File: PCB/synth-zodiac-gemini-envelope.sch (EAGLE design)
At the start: 23 parts, among them Q1 PNP, U1 TL074A

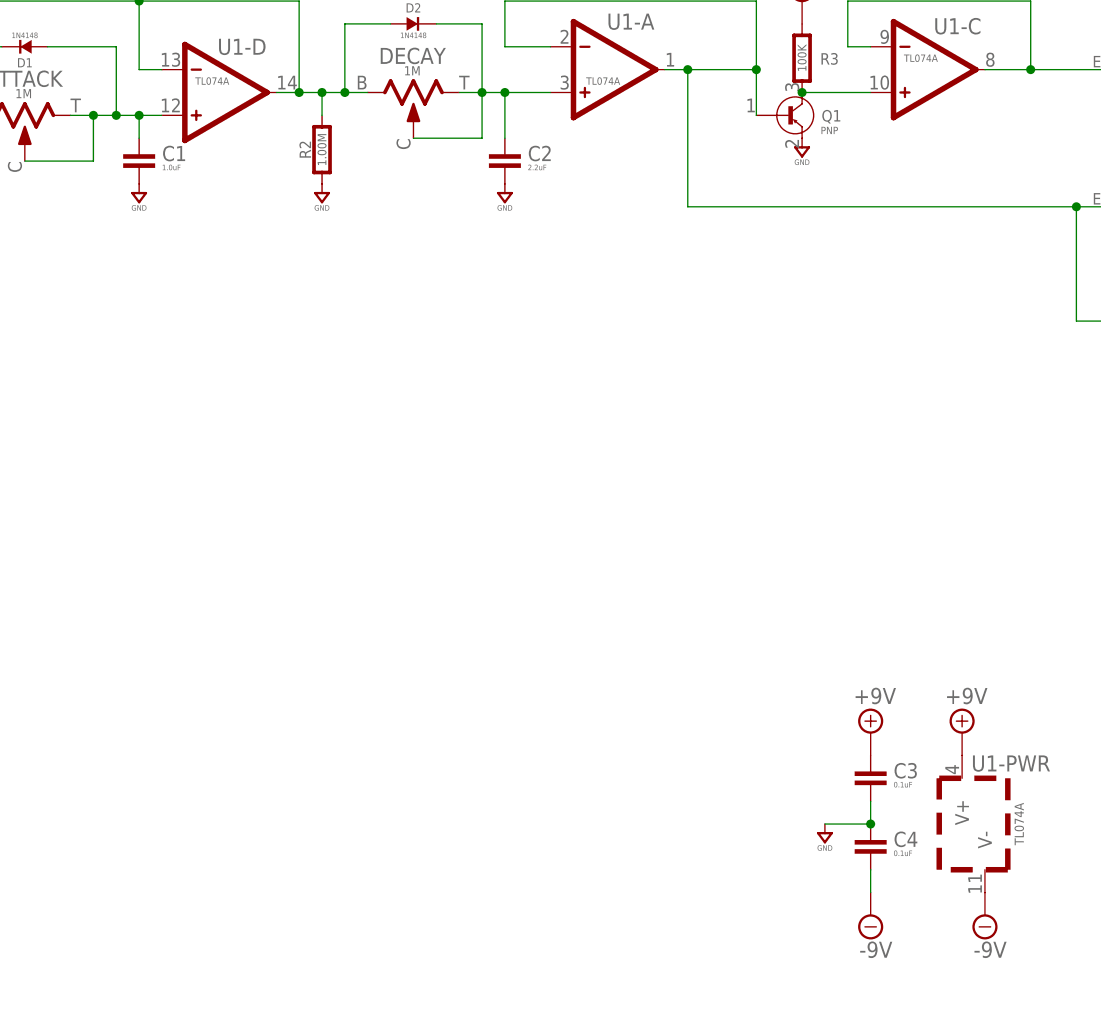
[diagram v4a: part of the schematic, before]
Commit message: Tune values and some schematic visual tweaks.
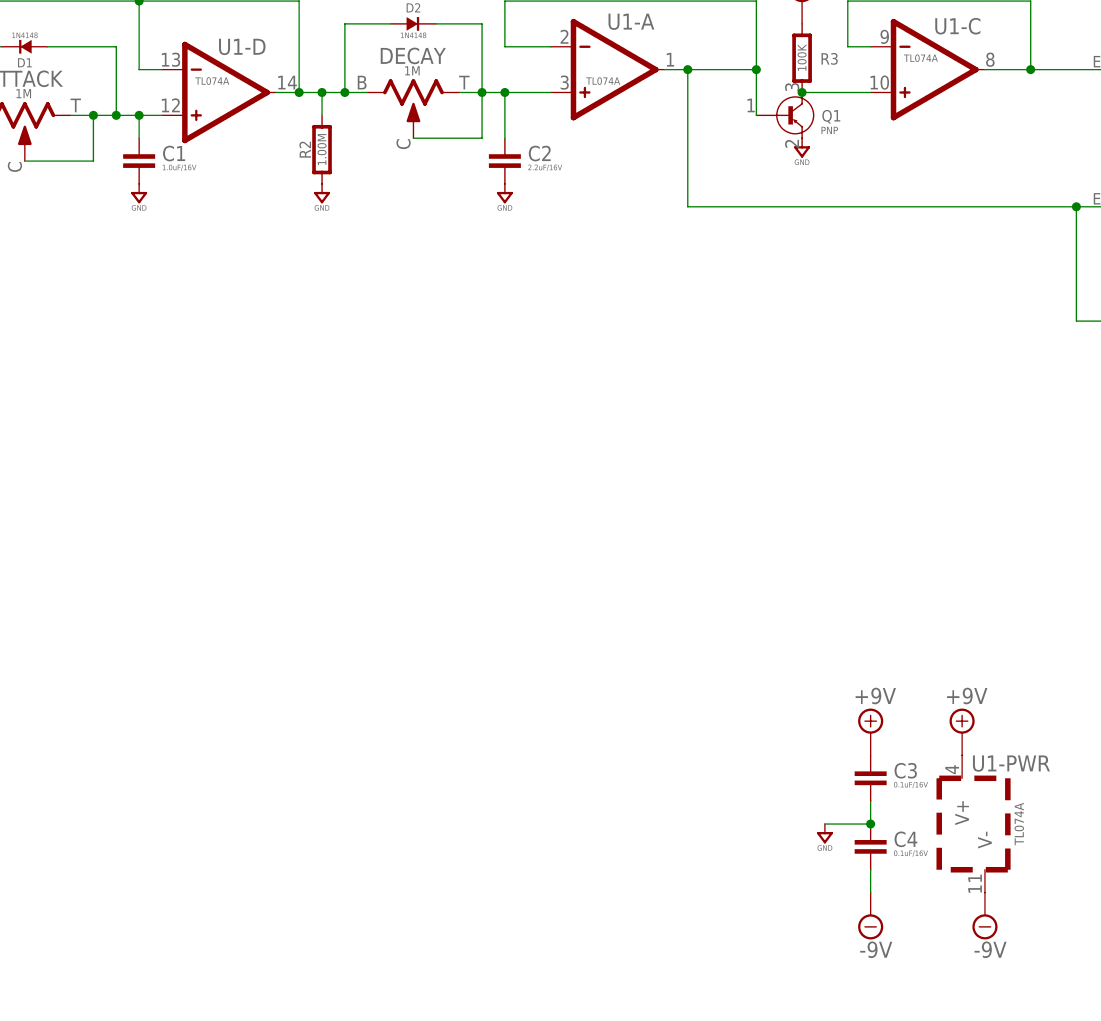
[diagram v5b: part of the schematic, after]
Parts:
- C1: value 1.0uF -> 1.0uF/16V
- C2: value 2.2uF -> 2.2uF/16V
- C3, C4: value 0.1uF -> 0.1uF/16V
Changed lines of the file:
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@@
 </part>
 <part name="U1" library="op-amp" library_urn="urn:adsk.eagle:library:7076615" deviceset="QUAD" device="TL074A-SOIC" package3d_urn="urn:adsk.eagle:package:7076665/2" value="TL074A"/>
-<part name="C1" library="rlc" library_urn="urn:adsk.eagle:library:4192893" deviceset="CAPACITOR" device="0603" package3d_urn="urn:adsk.eagle:package:4193021/4" value="1.0uF"/>
+<part name="C1" library="rlc" library_urn="urn:adsk.eagle:library:4192893" deviceset="CAPACITOR" device="0603" package3d_urn="urn:adsk.eagle:package:4193021/4" value="1.0uF/16V"/>
 <part name="R1" library="rlc" library_urn="urn:adsk.eagle:library:4192893" deviceset="RESISTOR" device="0603" package3d_urn="urn:adsk.eagle:package:4193040/5" value="1.00M"/>
 <part name="D1" library="diodes" library_urn="urn:adsk.eagle:library:7189447" deviceset="DIODE-" device="1N4148" package3d_urn="urn:adsk.eagle:package:7189471/3" value="1N4148"/>
@@
 <part name="SUPPLY157" library="supply" library_urn="urn:adsk.eagle:library:10485988" deviceset="GND" device=""/>
 <part name="D2" library="diodes" library_urn="urn:adsk.eagle:library:7189447" deviceset="DIODE-" device="1N4148" package3d_urn="urn:adsk.eagle:package:7189471/3" value="1N4148"/>
-<part name="C2" library="rlc" library_urn="urn:adsk.eagle:library:4192893" deviceset="CAPACITOR" device="0603" package3d_urn="urn:adsk.eagle:package:4193021/4" value="2.2uF"/>
+<part name="C2" library="rlc" library_urn="urn:adsk.eagle:library:4192893" deviceset="CAPACITOR" device="0603" package3d_urn="urn:adsk.eagle:package:4193021/4" value="2.2uF/16V"/>
 <part name="SUPPLY158" library="supply" library_urn="urn:adsk.eagle:library:10485988" deviceset="GND" device=""/>
 <part name="R3" library="rlc" library_urn="urn:adsk.eagle:library:4192893" deviceset="RESISTOR" device="0603" package3d_urn="urn:adsk.eagle:package:4193040/5" value="100K"/>
 <part name="SUPPLY159" library="supply" library_urn="urn:adsk.eagle:library:10485988" deviceset="GND" device=""/>
-<part name="C3" library="rlc" library_urn="urn:adsk.eagle:library:4192893" deviceset="CAPACITOR" device="0603" package3d_urn="urn:adsk.eagle:package:4193021/4" value="0.1uF"/>
-<part name="C4" library="rlc" library_urn="urn:adsk.eagle:library:4192893" deviceset="CAPACITOR" device="0603" package3d_urn="urn:adsk.eagle:package:4193021/4" value="0.1uF"/>
+<part name="C3" library="rlc" library_urn="urn:adsk.eagle:library:4192893" deviceset="CAPACITOR" device="0603" package3d_urn="urn:adsk.eagle:package:4193021/4" value="0.1uF/16V"/>
+<part name="C4" library="rlc" library_urn="urn:adsk.eagle:library:4192893" deviceset="CAPACITOR" device="0603" package3d_urn="urn:adsk.eagle:package:4193021/4" value="0.1uF/16V"/>
 <part name="SUPPLY161" library="supply" library_urn="urn:adsk.eagle:library:10485988" deviceset="GND" device=""/>
 <part name="SUPPLY153" library="supply" library_urn="urn:adsk.eagle:library:10485988" deviceset="+9V" device=""/>
